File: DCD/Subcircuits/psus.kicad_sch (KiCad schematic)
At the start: 36 parts, among them U1 TLV76780DBVR, U2 ADP7182AUJZ-1.8-R7, U3 LP2985-50DBVR, U4 LP2985-18DBVR, U5 LP2985-33DBVR

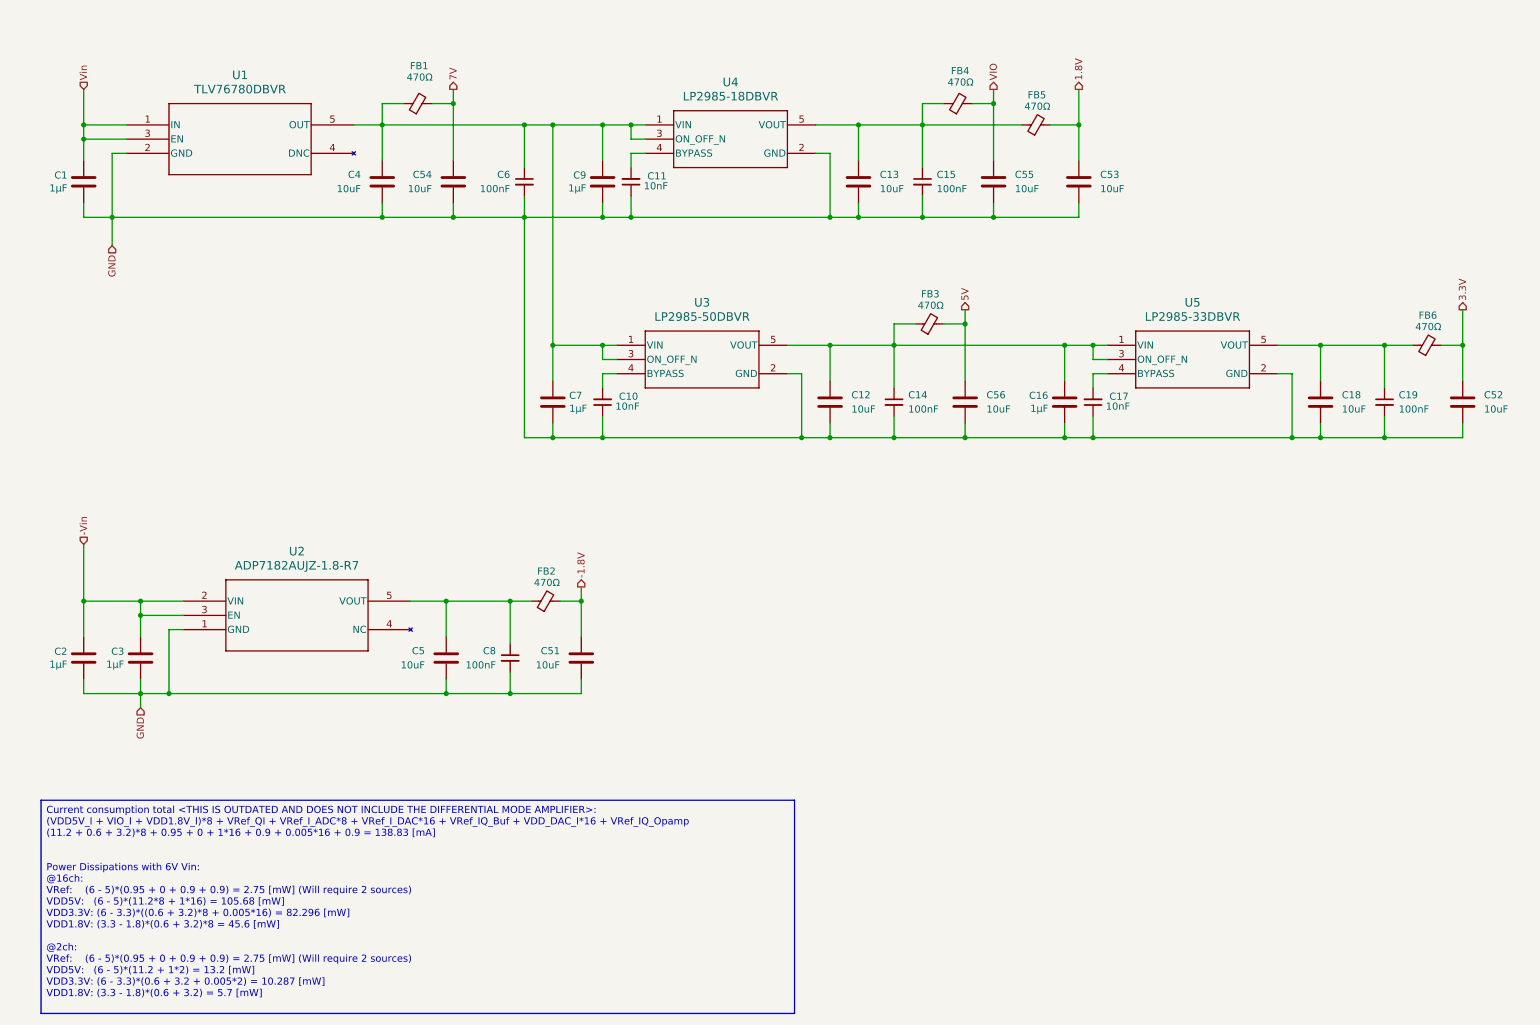
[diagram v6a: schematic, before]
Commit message: Schematics for the clock reconditioning
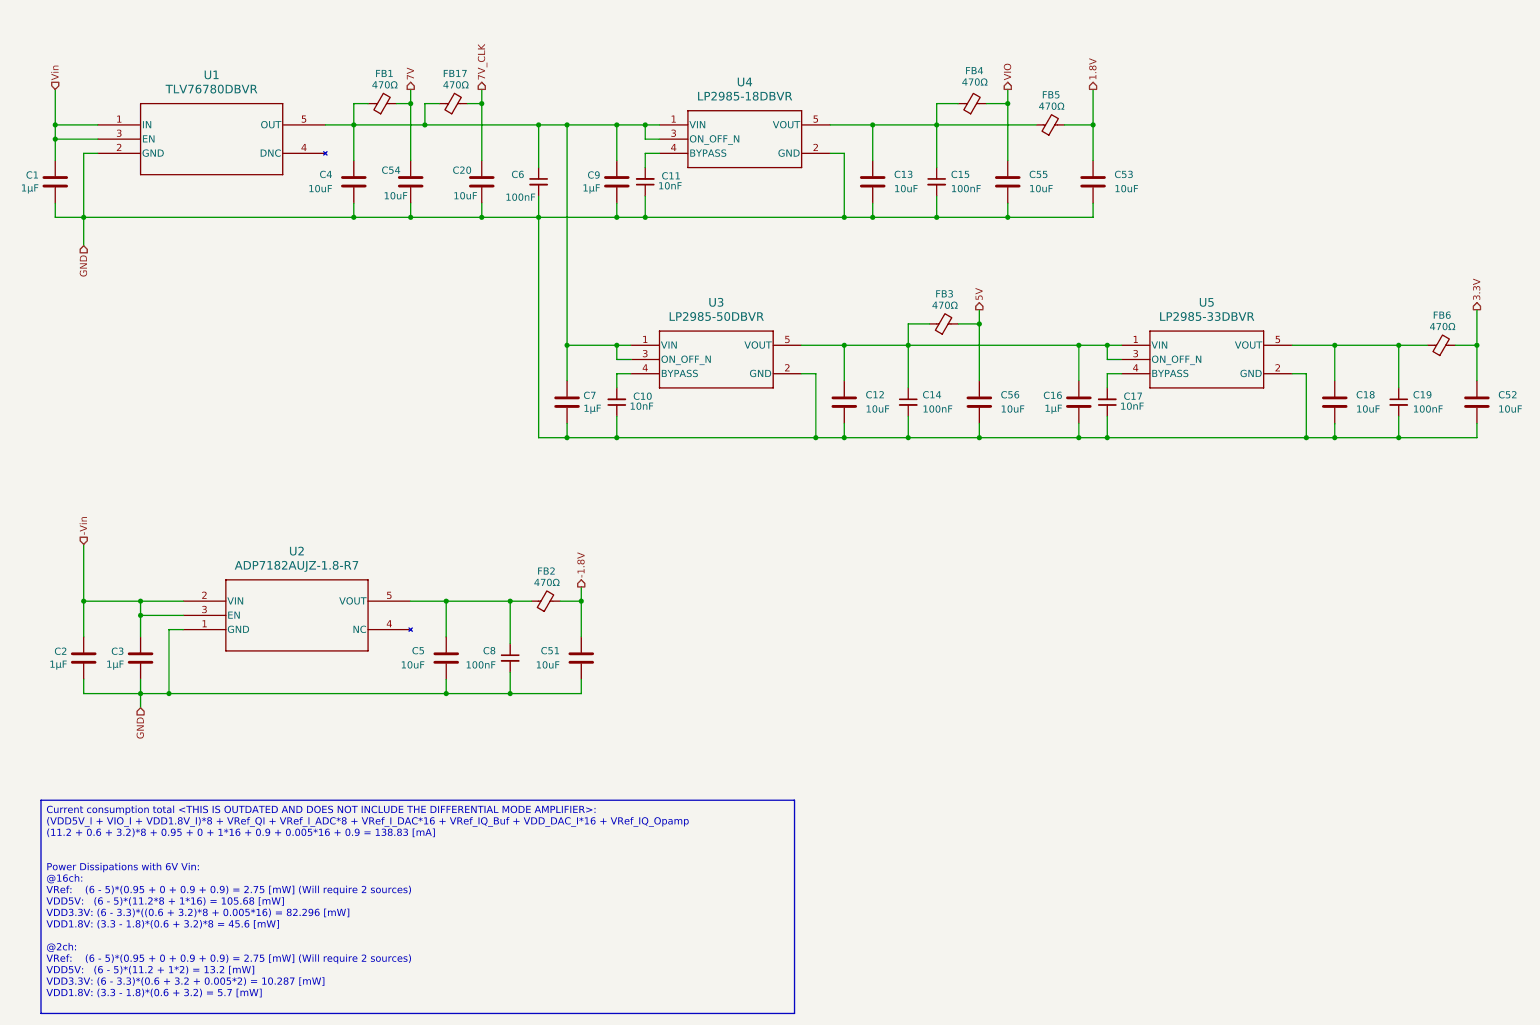
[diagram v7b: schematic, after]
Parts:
- added C20: 10uF, Capacitor_SMD:C_1210_3225Metric, symbol Device:C
- added FB17: 470Ω, Inductor_SMD:L_0603_1608Metric, symbol Device:FerriteBead_Small
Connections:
- net GND: now also C20.2
- net at C4.1, C6.1, C7.1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: now also FB17.1
- new net 7V_CLK: C20.1, FB17.2
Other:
- moved on the sheet: C1, C10, C11, C12, C13, C14, C15, C16, C17, C18, C19, C4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

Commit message: Added bodges
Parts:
- added D1: 1N4148WT, Diode_SMD:D_SOD-523, symbol Diode:1N4148WT
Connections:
- net GND: now also D1.1 (K); no longer U3.2 (GND)
- new net: D1.2 (A), U3.2 (GND)
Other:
- note added: "This should be 5.5V"
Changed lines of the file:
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@@
 	(generator_version "9.0")
 	(paper "A4")
+	(text "This should be 5.5V"
+		(exclude_from_sim no)
+		(at 142.24 85.598 0)
+		(effects
+			(font
+				(size 1.27 1.27)
+			)
+		)
+	)
 	(text_box "Current consumption total <THIS IS OUTDATED AND DOES NOT INCLUDE THE DIFFERENTIAL MODE AMPLIFIER>:\n(VDD5V_I + VIO_I + VDD1.8V_I)*8 + VRef_QI + VRef_I_ADC*8 + VRef_I_DAC*16 + VRef_IQ_Buf + VDD_DAC_I*16 + VRef_IQ_Opamp\n(11.2 + 0.6 + 3.2)*8 + 0.95 + 0 + 1*16 + 0.9 + 0.005*16 + 0.9 = 138.83 [mA]\n\n\nPower Dissipations with 6V Vin:\n @16ch:\n  VRef:    (6 - 5)*(0.95 + 0 + 0.9 + 0.9) = 2.75 [mW] (Will require 2 sources)\n  VDD5V:   (6 - 5)*(11.2*8 + 1*16) = 105.68 [mW]\n  VDD3.3V: (6 - 3.3)*((0.6 + 3.2)*8 + 0.005*16) = 82.296 [mW]\n  VDD1.8V: (3.3 - 1.8)*(0.6 + 3.2)*8 = 45.6 [mW]\n\n@2ch:\n  VRef:    (6 - 5)*(0.95 + 0 + 0.9 + 0.9) = 2.75 [mW] (Will require 2 sources)\n  VDD5V:   (6 - 5)*(11.2 + 1*2) = 13.2 [mW]\n  VDD3.3V: (6 - 3.3)*(0.6 + 3.2 + 0.005*2) = 10.287 [mW]\n  VDD1.8V: (3.3 - 1.8)*(0.6 + 3.2) = 5.7 [mW]"
 		(exclude_from_sim no)
@@
 	(wire
 		(pts
+			(xy 156.21 80.01) (xy 156.21 78.74)
+		)
+		(stroke
+			(width 0)
+			(type default)
+		)
+	)
+	(wire
+		(pts
 			(xy 114.3 133.35) (xy 114.3 135.89)
 		)
@@
 	(wire
 		(pts
-			(xy 156.21 90.17) (xy 156.21 78.74)
+			(xy 156.21 90.17) (xy 156.21 87.63)
 		)
 		(stroke
@@
 					(unit 1)
 				)
+			)
+		)
+	)
+	(symbol
+		(lib_id "Diode:1N4148WT")
+		(at 156.21 83.82 270)
+		(mirror x)
+		(unit 1)
+		(exclude_from_sim no)
+		(in_bom yes)
+		(on_board yes)
+		(dnp no)
+		(property "Reference" "D1"
+			(at 155.194 81.026 90)
+			(effects
+				(font
+					(size 1.27 1.27)
+				)
+				(justify right)
+			)
+		)
+		(property "Value" "1N4148WT"
+			(at 153.67 85.0899 90)
+			(effects
+				(font
+					(size 1.27 1.27)
+				)
+				(justify right)
+				(hide yes)
+			)
+		)
+		(property "Footprint" "Diode_SMD:D_SOD-523"
+			(at 151.765 83.82 0)
+			(effects
+				(font
+					(size 1.27 1.27)
+				)
+				(hide yes)
+			)
+		)
+		(property "Datasheet" "https://www.diodes.com/assets/Datasheets/ds30396.pdf"
+			(at 156.21 83.82 0)
+			(effects
+				(font
+					(size 1.27 1.27)
+				)
+				(hide yes)
+			)
+		)
+		(property "Description" "75V 0.15A Fast switching Diode, SOD-523"
+			(at 156.21 83.82 0)
+			(effects
+				(font
+					(size 1.27 1.27)
+				)
+				(hide yes)
+			)
+		)
+		(property "Sim.Device" "D"
+			(at 156.21 83.82 0)
+			(effects
+				(font
+					(size 1.27 1.27)
+				)
+				(hide yes)
+			)
+		)
+		(property "Sim.Pins" "1=K 2=A"
+			(at 156.21 83.82 0)
+			(effects
+				(font
+					(size 1.27 1.27)
+				)
+				(hide yes)
+			)
+		)
+		(pin "2"
+		)
+		(pin "1"
+		)
+		(instances
+			(project ""
+				(path "/b8e3d55b-fa56-4199-88ad-60cfd98f56f9/84a1e6aa-eb06-44a1-ae19-b2ac56cdff0b"
+					(reference "D1")
+					(unit 1)
+				)
